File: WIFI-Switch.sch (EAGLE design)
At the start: 23 parts, among them T1 BT136/138/139, U1 AMS1117

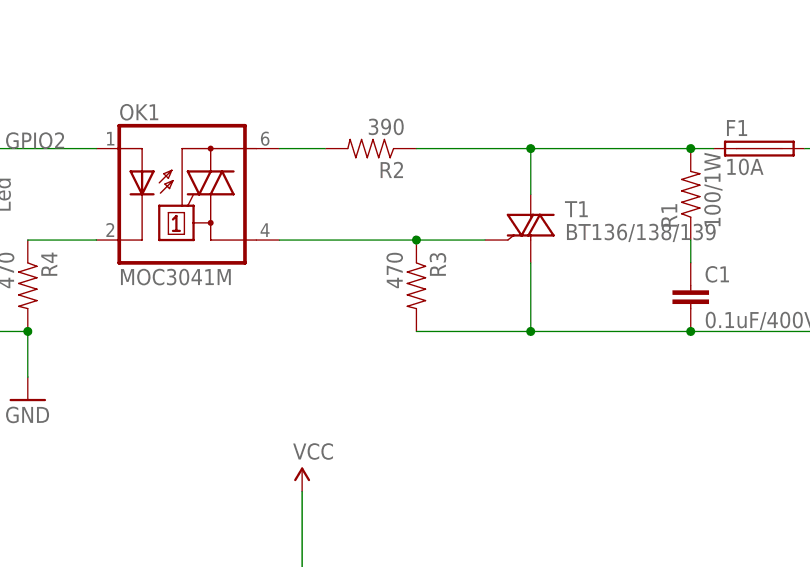
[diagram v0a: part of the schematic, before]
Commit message: update board size
update board size and components reposition
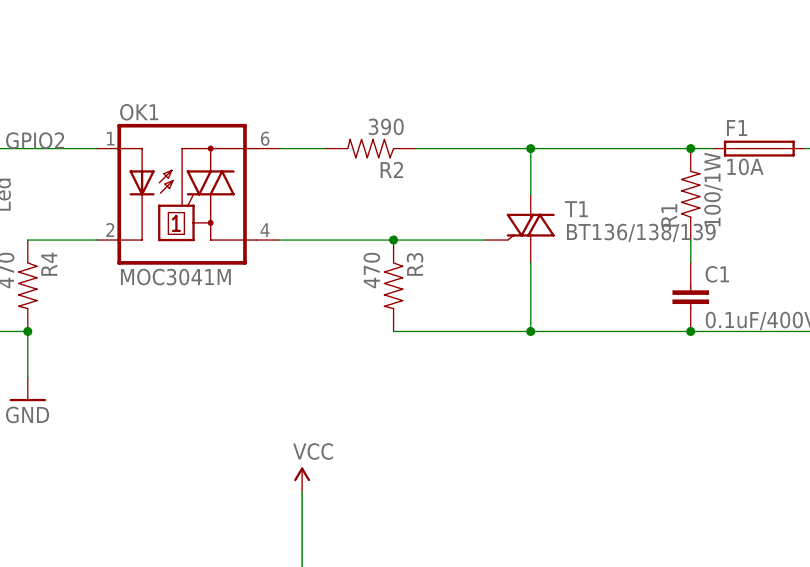
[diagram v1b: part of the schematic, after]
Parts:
- R3: device SparkFun-Resistors:RESISTORPTH-1/4W-VERT -> SparkFun-Resistors:RESISTORPTH-1/4W
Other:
- moved on the sheet: R3
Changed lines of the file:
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@@
 <part name="R1" library="SparkFun-Resistors" deviceset="RESISTOR" device="PTH-2W" value="100/1W"/>
 <part name="R2" library="SparkFun-Resistors" deviceset="RESISTOR" device="PTH-1/4W-VERT" value="390"/>
-<part name="R3" library="SparkFun-Resistors" deviceset="RESISTOR" device="PTH-1/4W-VERT" value="470"/>
+<part name="R3" library="SparkFun-Resistors" deviceset="RESISTOR" device="PTH-1/4W" value="470"/>
 <part name="R4" library="SparkFun-Resistors" deviceset="RESISTOR" device="PTH-1/4W-VERT" value="470"/>
 <part name="R5" library="SparkFun-Resistors" deviceset="RESISTOR" device="PTH-1/4W-VERT" value="470"/>
@@
 <instance part="R1" gate="G$1" x="177.8" y="127" rot="R90"/>
 <instance part="R2" gate="G$1" x="142.24" y="132.08" rot="R180"/>
-<instance part="R3" gate="G$1" x="147.32" y="116.84" rot="R270"/>
+<instance part="R3" gate="G$1" x="144.78" y="116.84" rot="R270"/>
 <instance part="R4" gate="G$1" x="104.14" y="116.84" rot="R270"/>
 <instance part="R5" gate="G$1" x="96.52" y="116.84" rot="R270"/>
@@
 <pinref part="OK1" gate="-1" pin="A1"/>
 <pinref part="R3" gate="G$1" pin="1"/>
-<wire x1="132.08" y1="121.92" x2="147.32" y2="121.92" width="0.1524" layer="91"/>
+<wire x1="132.08" y1="121.92" x2="144.78" y2="121.92" width="0.1524" layer="91"/>
 <pinref part="T1" gate="G$1" pin="G"/>
-<wire x1="147.32" y1="121.92" x2="154.94" y2="121.92" width="0.1524" layer="91"/>
-<junction x="147.32" y="121.92"/>
+<wire x1="144.78" y1="121.92" x2="154.94" y2="121.92" width="0.1524" layer="91"/>
+<junction x="144.78" y="121.92"/>
 </segment>
 </net>
@@
 <wire x1="160.02" y1="119.38" x2="160.02" y2="111.76" width="0.1524" layer="91"/>
 <pinref part="R3" gate="G$1" pin="2"/>
-<wire x1="160.02" y1="111.76" x2="147.32" y2="111.76" width="0.1524" layer="91"/>
+<wire x1="160.02" y1="111.76" x2="144.78" y2="111.76" width="0.1524" layer="91"/>
 <pinref part="C1" gate="G$1" pin="2"/>
 <wire x1="160.02" y1="111.76" x2="177.8" y2="111.76" width="0.1524" layer="91"/>
